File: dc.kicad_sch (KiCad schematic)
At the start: 24 parts, among them J9 J_PWR_11-25V, U1 LDO_3V3_ISO, U2 NCM3S1205MC, U3 NCM3S1205MC

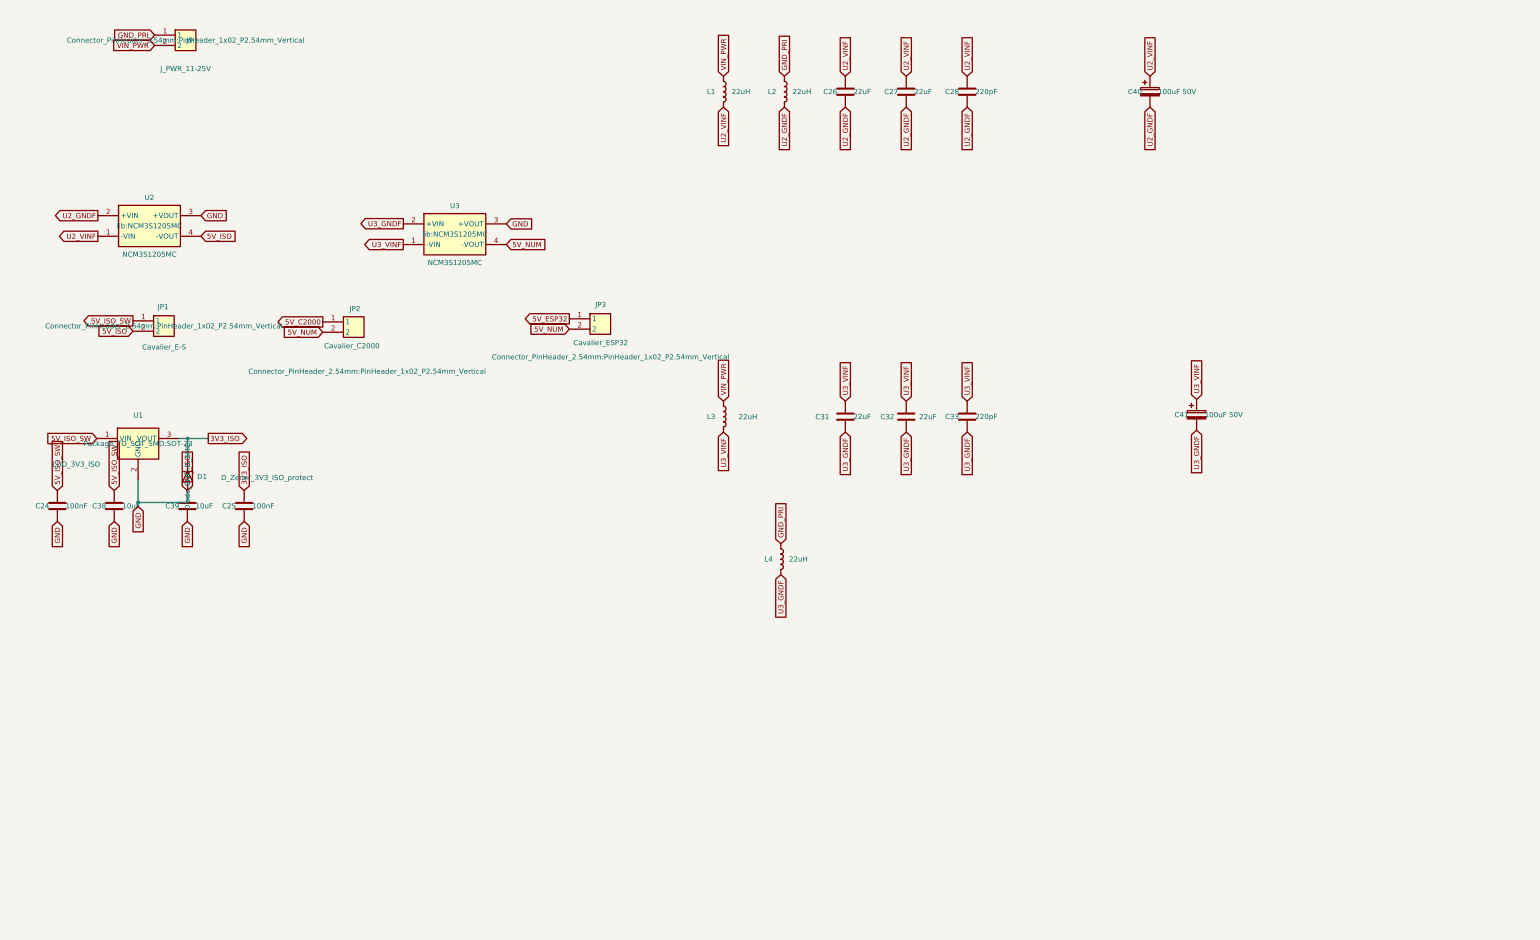
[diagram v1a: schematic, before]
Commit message: Ajoute le filtre EMC FL3/FL4 (U3), corrige les caps de sortie 100uF et le rendu 3D du devkit/NCM3S1205MC
- dc.kicad_sch : ajoute FL3/FL4 (Bourns SRF0905) sur le filtre EMC de
  U3, empreinte lib:Filter_Bourns_SRF0905_6.0x9.2mm_My
- connecteur_devkit.kicad_sch : C36/C37 renommes C59/C60, passent en
  100uF 50V / CP_Elec_8x10.5 (electrolytique) au lieu du MLCC 1210 ;
  embases devkit en PinSocket (femelle) au lieu de PinHeader
- connecteurs_nappe/protection_nappe.kicad_sch : complete les labels
  nappe manquants (Discharge, PWM3_B, PWM4_B, Stage2_EN)
- lib/ER-OLEDM032-1.kicad_mod, lib/NCM3S1205MC.kicad_mod : corrige
  l'orientation/offset des modeles 3D (STEP mal aligne)
- lib/DLW5BSZ801TQ2L.step : nouveau modele 3D
- shield.kicad_pcb/.kicad_pro : presets de piste/via supplementaires,
  remove_islands actif
- README.md + doc/shield.png : ajoute le rendu 3D de la carte

Verification avant commit : kicad-cli sch erc (233 violations, 35
erreurs) et pcb drc (329 violations + 183 non connectes) --
inchange dans sa nature par rapport aux sessions precedentes, rien
corrige ici qui ne decoule pas des changements ci-dessus (regle
KICAD.md : rapporter, pas corriger d'office).

Co-Authored-By: Claude Sonnet 5 <noreply@anthropic.com>
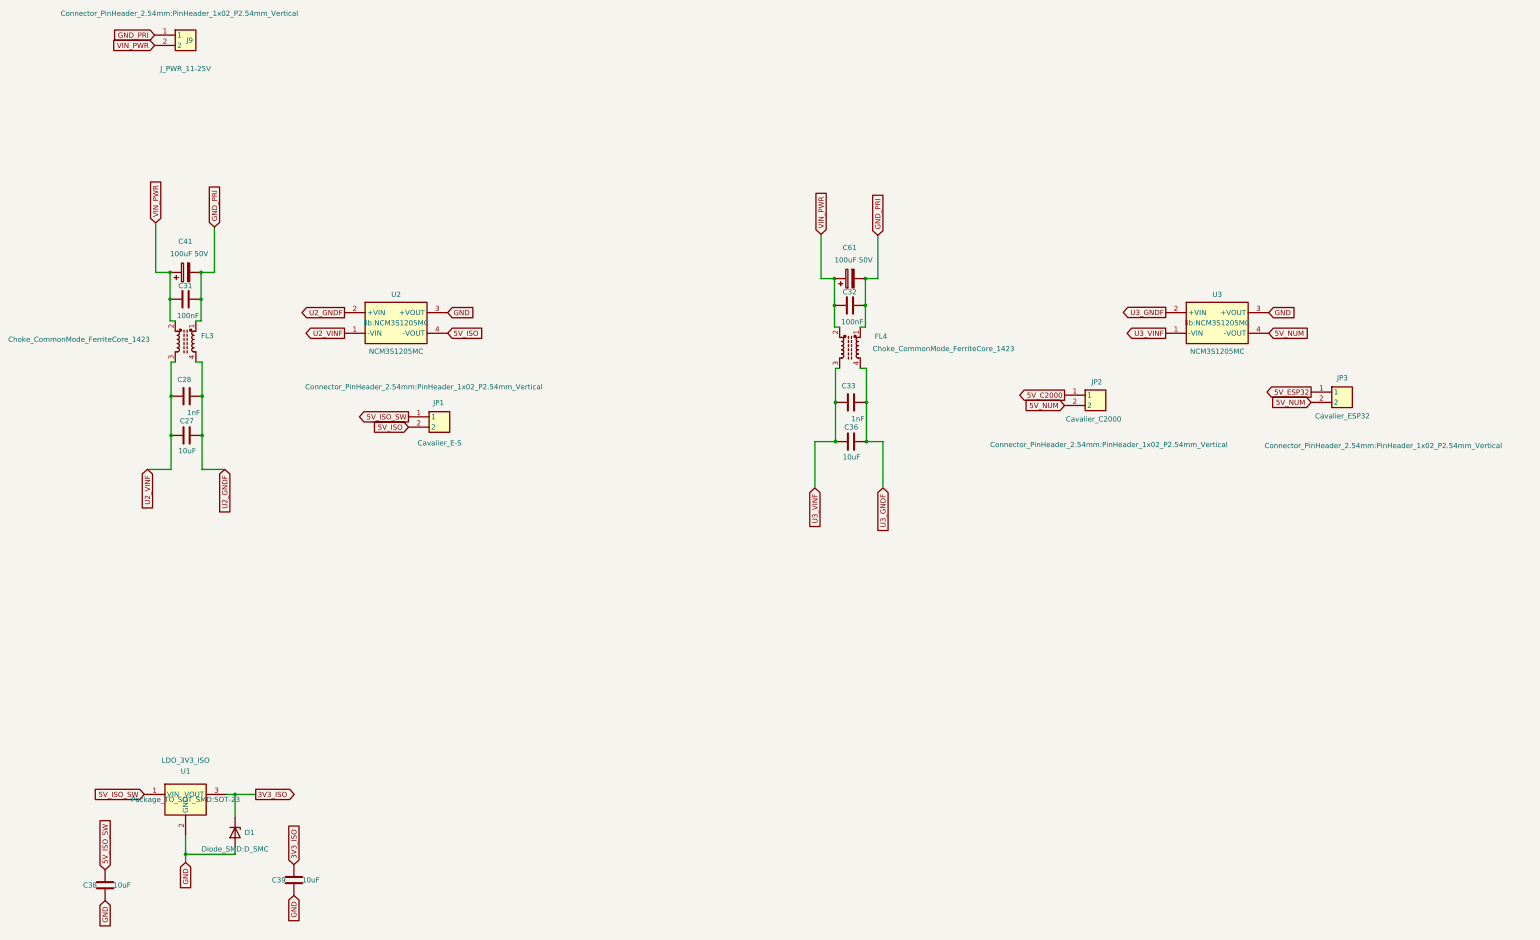
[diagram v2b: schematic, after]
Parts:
- removed C24, C25: 100nF, Capacitor_SMD:C_0805_2012Metric, symbol Device:C
- removed C26: 22uF, Capacitor_SMD:C_0805_2012Metric, symbol Device:C
- removed C40: 100uF 50V, Capacitor_SMD:CP_Elec_8x10.5, symbol Device:C_Polarized
- removed L1, L2, L3, L4: 22uH, Inductor_SMD:L_0805_2012Metric, symbol Device:L
- added C36: 10uF, Capacitor_SMD:C_0805_2012Metric, symbol Device:C
- added C61: 100uF 50V, Capacitor_SMD:CP_Elec_8x10.5, symbol Device:C_Polarized
- added FL3, FL4: Choke_CommonMode_FerriteCore_1423, lib:Filter_Bourns_SRF0905_6.0x9.2mm_My, symbol Filter:Choke_CommonMode_FerriteCore_1423
- C27: value 22uF -> 10uF
- C28, C33: value 220pF -> 1nF
- C31, C32: value 22uF -> 100nF
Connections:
- net GND_PRI: now also C31.2, C32.2, C41.2, C61.2, FL3.1, FL4.1
- net U2_GNDF: now also C27.1, FL3.4; no longer C27.2
- net U2_VINF: now also C27.2, FL3.3; no longer C27.1
- net U3_GNDF: now also C36.1, FL4.4; no longer C31.2, C32.2, C41.2
- net U3_VINF: now also C36.2, FL4.3; no longer C31.1, C32.1, C41.1
- net VIN_PWR: now also C31.1, C32.1, C41.1, C61.1, FL3.2, FL4.2
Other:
- moved on the sheet: C27, C28, C38, C39, C41, D1, JP1, JP2, JP3, U1, U2, U3
